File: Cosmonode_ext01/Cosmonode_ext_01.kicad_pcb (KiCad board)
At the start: 2 copper layers, 19.7 x 31.1 mm, 15 parts, among them J1 GS2, J2 GS3, J3 CONN_01X07, J5 CONN_01X07, J7 GS3, J8 GS3, J9 GS3, U1 TSL2561T(6P-3.8X2.6MM), U2 BMP180, U3 SI7020-A20-YM0R

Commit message: fully update to v0.3
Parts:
- removed J2, J7: GS3, Connectors:GS3
- added J4: Aloes_Logo, Aloes:Aloes_mini, F.Cu at (167.6, 130.8)
- added J6: OSHW_Logo, Symbols:OSHW-Logo_5.7x6mm_SilkScreen, B.Cu at (168.3, 111.1)
- J3, J5: value CONN_01X07 -> CONN_01X08; footprint Pin_Headers:Pin_Header_Straight_1x07_Pitch2.54mm -> Socket_Strips:Socket_Strip_Straight_1x08_Pitch2.54mm
- U1: footprint TSL2561T_6P-3.8X2.6MM_:TMB6-1.55-3.8X2.6MM -> TSL2561T:TMB6-1.55-3.8X2.6MM
- moved J9 13.1 mm to (180.3, 122.6)
- moved U2 10.2 mm to (167.6, 123.8)
- moved J8 8.52 mm to (184.8, 122.6), turned to 0 degrees
- moved C2 5.46 mm to (175.9, 123.8), turned to 90 degrees
- moved J3 5.24 mm to (167.6, 135.9)
- moved C1 3.70 mm to (174.6, 113.0)
- moved U3 3.70 mm to (179.7, 113.0)
- moved J1 3.17 mm to (167.0, 117.5)
- moved U1 2.84 mm to (170.2, 113.0)
- moved C3 2.84 mm to (184.2, 113.0), turned to 90 degrees
- moved R1 2.62 mm to (172.1, 117.5), turned to 0 degrees
- moved J5 2.29 mm to (167.6, 105.4)
- moved C4 0.90 mm to (172.1, 123.8), turned to 90 degrees
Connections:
- C2 pad 1: Net-(C2-Pad1) -> Net-(C1-Pad1)
- C3 pad 1: Net-(C3-Pad1) -> Net-(C1-Pad1)
- C4 pad 1: Net-(C2-Pad1) -> Net-(C1-Pad1)
- J9 pad 2: Net-(C3-Pad1) -> Net-(C1-Pad1)
- U2 pad 2: Net-(C2-Pad1) -> Net-(C1-Pad1)
- U2 pad 3: Net-(C2-Pad1) -> Net-(C1-Pad1)
- U3 pad 5: Net-(C3-Pad1) -> Net-(C1-Pad1)
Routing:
- net Net-(C1-Pad2): track 54.3 -> 9.35 mm, vias 0 -> 9
- net +3V3: track 62.2 -> 21.6 mm, vias 1 -> 0
- net Net-(C1-Pad1): track 13.5 -> 52.7 mm
- net /D5: track 15.5 -> 0.00 mm
- net Net-(C2-Pad1): track 14.5 -> 0.00 mm
- net /D3: track 42.3 -> 28.1 mm
- net Net-(C3-Pad1): track 12.7 -> 0.00 mm
- net GND: track 18.6 -> 26.5 mm, vias 1 -> 0
- net /A4: track 37.5 -> 45.1 mm
- net /A5: track 42.7 -> 35.6 mm, vias 0 -> 1
- net /D7: track 6.81 -> 0.00 mm
- net /D4: track 22.1 -> 16.3 mm, vias 1 -> 0
- net /D6: track 12.3 -> 16.0 mm, vias 1 -> 0
- added copper zone on B.Cu, net Net-(C1-Pad2)
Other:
- board size 19.7 x 31.1 mm -> 23.5 x 35.6 mm
- board text added: "+3V3"
- board text added: "1"
- board text added: "A6"
- board text added: "A7"
- board text added: "ALOES.IO"
- board text added: "Extension #1 TSL2561 BMP180 Si7021"
- board text removed: "+3.3V"
- board text removed: "3.3V"

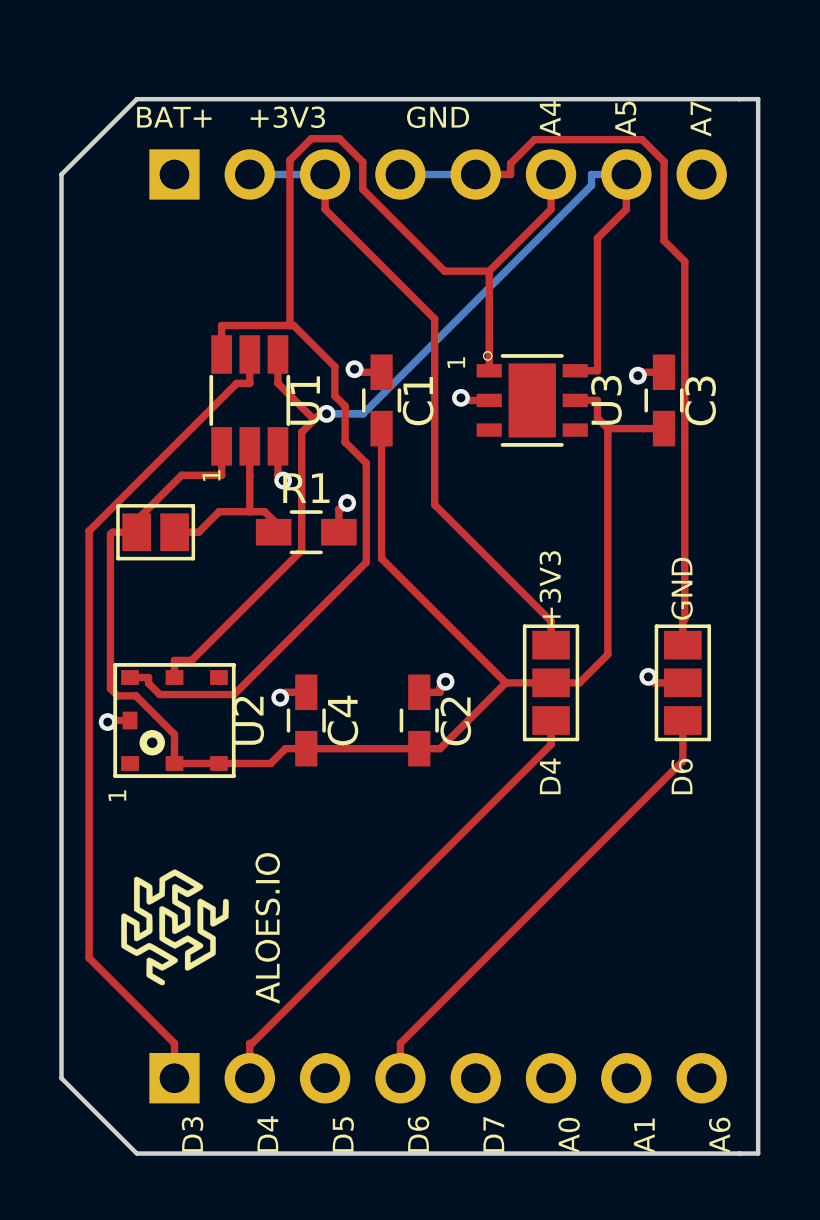
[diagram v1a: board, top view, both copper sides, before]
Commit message: update to v0.5 ( base, ext05, ext07, ext08 )
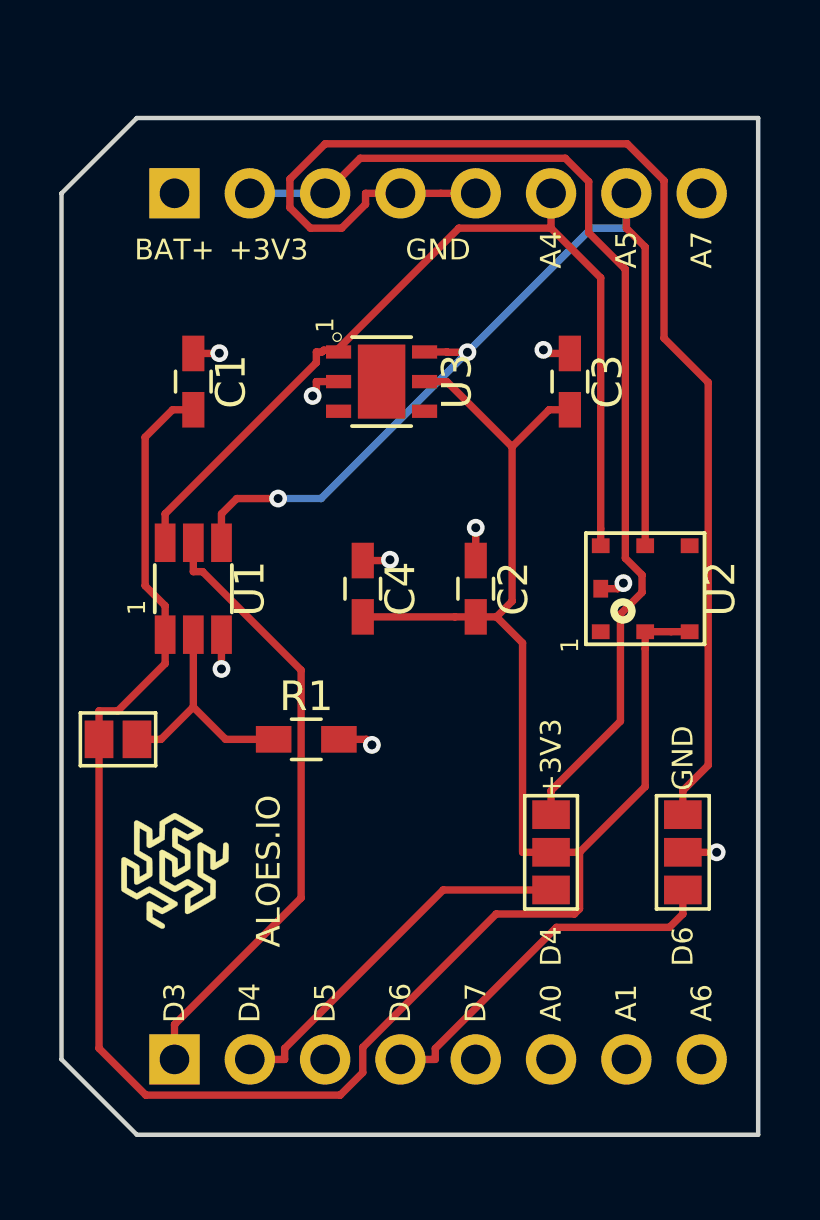
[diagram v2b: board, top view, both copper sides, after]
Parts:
- moved U2 16.5 mm to (183.5, 119.4)
- moved J1 7.10 mm to (165.7, 124.5)
- moved R1 6.98 mm to (172.1, 124.5)
- moved U1 6.63 mm to (168.3, 119.4)
- moved C1 6.38 mm to (168.3, 112.4)
- moved J8 5.72 mm to (184.8, 128.3)
- moved J9 5.72 mm to (180.3, 128.3)
- moved U3 5.12 mm to (174.6, 112.4)
- moved C2 4.84 mm to (177.8, 119.4)
- moved C4 4.84 mm to (174.0, 119.4)
- moved C3 3.24 mm to (181.0, 112.4)
- moved J4 1.91 mm to (167.6, 128.9)
- moved J5 0.64 mm to (167.6, 106.0)
- moved J3 0.63 mm to (167.6, 135.3)
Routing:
- net Net-(C1-Pad1): track 52.7 -> 82.9 mm
- net GND: track 26.5 -> 44.2 mm
- net /A4: track 45.1 -> 30.9 mm
- net +3V3: track 21.6 -> 35.6 mm
- net /D3: track 28.1 -> 20.9 mm
- net /D4: track 16.3 -> 12.7 mm
- net /D6: track 16.0 -> 12.6 mm
- net /A5: track 35.6 -> 33.4 mm, vias 1 -> 2
- net Net-(J1-Pad2): track 6.34 -> 7.95 mm
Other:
- board size 23.5 x 35.6 mm -> 23.5 x 34.3 mm
